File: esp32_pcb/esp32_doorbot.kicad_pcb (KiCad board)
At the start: 2 copper layers, 29.2 x 51.8 mm, 20 parts, among them J1 Conn_01x07_Male, J2 Conn_01x02_Female, J3 Barrel_Jack, J4 WROOM32_1, J5 WROOM32_2, Q1 ZXMP4A16G, U1 L7805

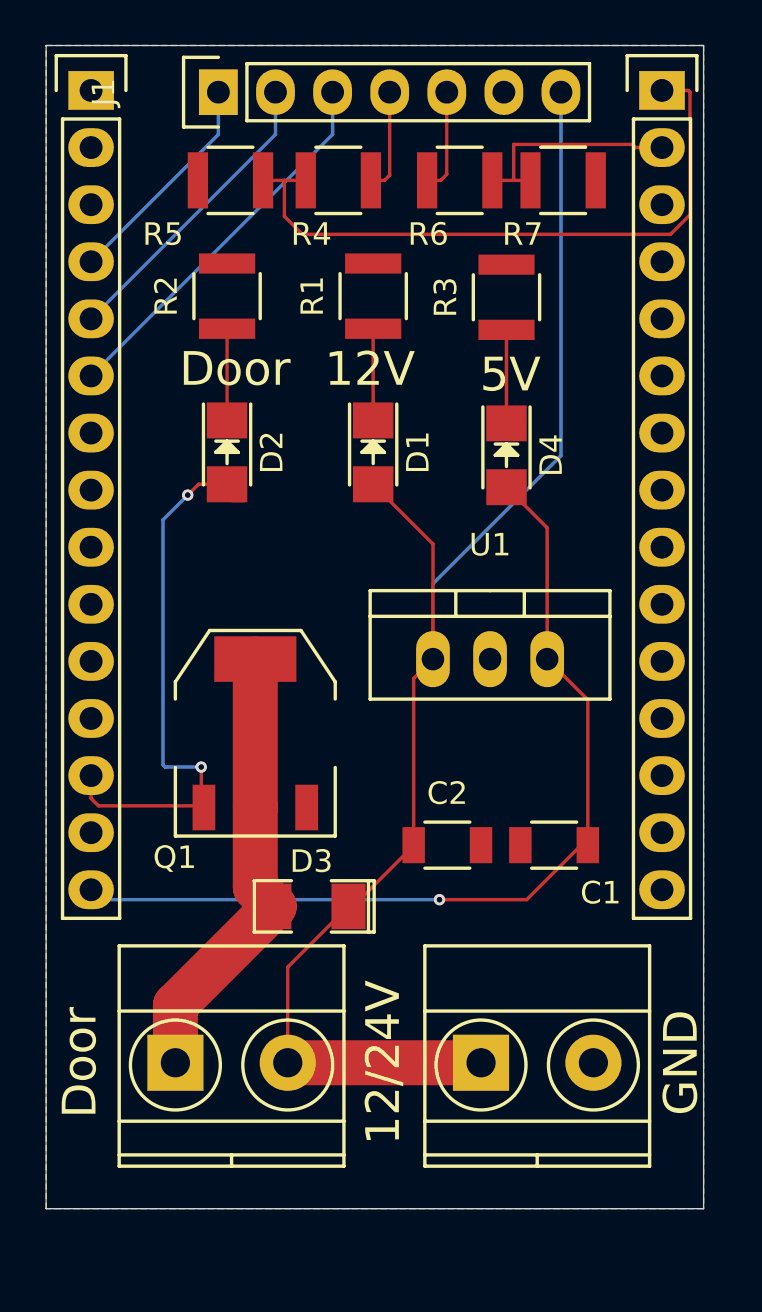
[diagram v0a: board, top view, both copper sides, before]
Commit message: Convert power screw terminal into barrel jack. Convert back pin header to proper JST-ZH connector.
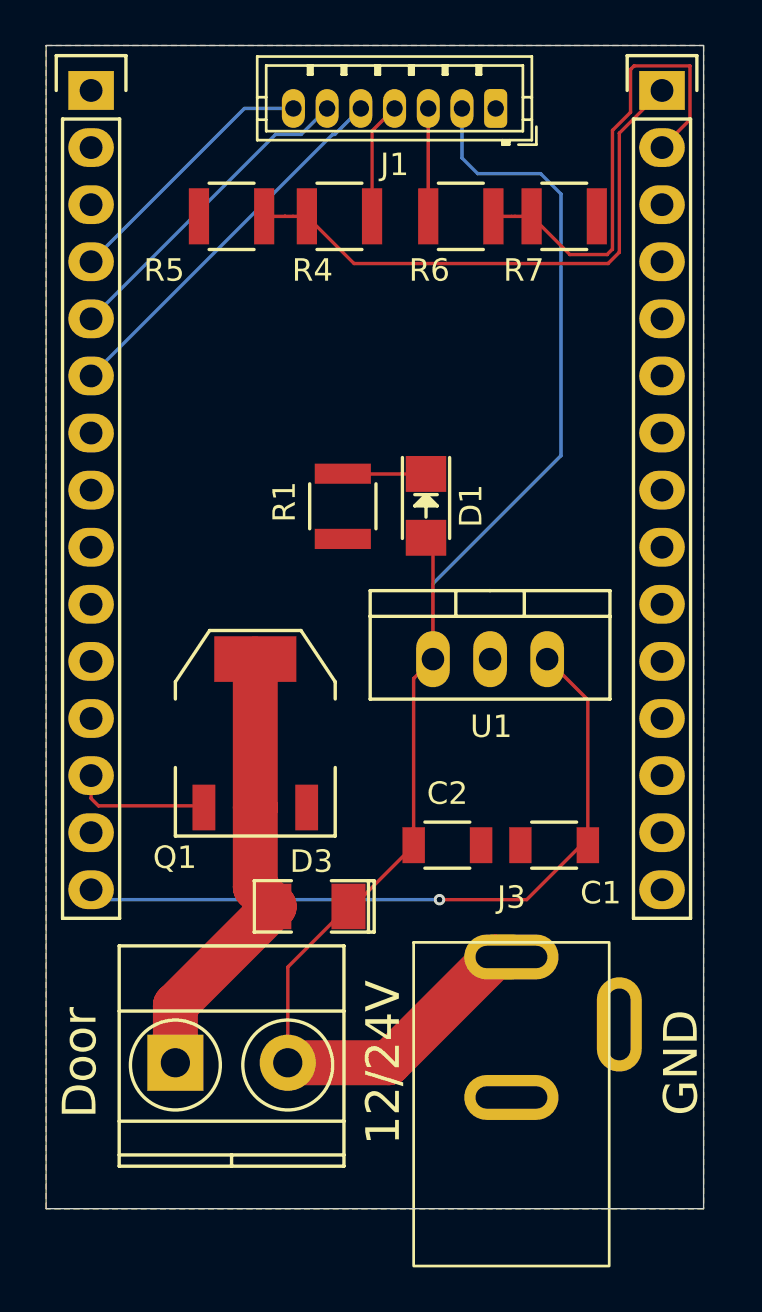
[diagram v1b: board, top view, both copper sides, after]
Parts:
- removed D2, D4: LED, LEDs:LED-1206
- removed R2, R3: 1K, Resistors_SMD:R_1210
- added REF**: Polarity_Center_Positive_6mm_SilkScreen, Symbol:Polarity_Center_Positive_6mm_SilkScreen, B.Cu at (111.2, 128.0)
- J1: footprint Pin_Headers:Pin_Header_Straight_1x07 -> Connector_JST:JST_ZH_B7B-ZR_1x07_P1.50mm_Vertical
- J3: footprint Terminal_Blocks:TerminalBlock_Pheonix_MKDS1.5-2pol -> esp32_doorbot:Tensility 54-00166
- Q1: value ZXMP4A16G -> NDT3055
- R1: value 1K -> 2K
- moved J1 12.4 mm to (118.0, 100.8), turned to 180 degrees
- moved R1 9.45 mm to (111.2, 118.5), turned to -90 degrees
- moved J3 9.14 mm to (118.7, 152.3)
- moved D1 3.34 mm to (114.9, 118.5)
- moved R4 1.60 mm to (111.0, 105.6)
- moved R5 1.60 mm to (106.2, 105.6)
- moved R6 1.60 mm to (116.5, 105.6)
- moved R7 1.60 mm to (121.0, 105.6)
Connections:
- J1 pad 1: 24_32_SWITCH -> GND
- J1 pad 2: READER_LED -> 12V
- J1 pad 3: READER_BUZZ -> WIEGAND_IN1
- J1 pad 5: WIEGAND_IN1 -> READER_BUZZ
- J1 pad 6: GND -> READER_LED
- J1 pad 7: 12V -> 24_32_SWITCH
- J4 pad 1: Net-(J4-Pad1) -> unconnected-(J4-Pin_1-Pad1)
- J4 pad 10: Net-(J4-Pad10) -> unconnected-(J4-Pin_10-Pad10)
- J4 pad 11: Net-(J4-Pad11) -> unconnected-(J4-Pin_11-Pad11)
- J4 pad 12: Net-(J4-Pad12) -> unconnected-(J4-Pin_12-Pad12)
- J4 pad 2: Net-(J4-Pad2) -> unconnected-(J4-Pin_2-Pad2)
- J4 pad 3: Net-(J4-Pad3) -> unconnected-(J4-Pin_3-Pad3)
- J4 pad 7: Net-(J4-Pad7) -> unconnected-(J4-Pin_7-Pad7)
- J4 pad 8: Net-(J4-Pad8) -> unconnected-(J4-Pin_8-Pad8)
- J4 pad 9: Net-(J4-Pad9) -> unconnected-(J4-Pin_9-Pad9)
- J5 pad 10: Net-(J5-Pad10) -> unconnected-(J5-Pin_10-Pad10)
- J5 pad 11: Net-(J5-Pad11) -> unconnected-(J5-Pin_11-Pad11)
- J5 pad 12: Net-(J5-Pad12) -> unconnected-(J5-Pin_12-Pad12)
- J5 pad 13: Net-(J5-Pad13) -> unconnected-(J5-Pin_13-Pad13)
- J5 pad 15: Net-(J5-Pad15) -> unconnected-(J5-Pin_15-Pad15)
- J5 pad 3: Net-(J5-Pad3) -> unconnected-(J5-Pin_3-Pad3)
- J5 pad 4: Net-(J5-Pad4) -> unconnected-(J5-Pin_4-Pad4)
- J5 pad 5: Net-(J5-Pad5) -> unconnected-(J5-Pin_5-Pad5)
- J5 pad 6: Net-(J5-Pad6) -> unconnected-(J5-Pin_6-Pad6)
- J5 pad 7: Net-(J5-Pad7) -> unconnected-(J5-Pin_7-Pad7)
- J5 pad 8: Net-(J5-Pad8) -> unconnected-(J5-Pin_8-Pad8)
- J5 pad 9: Net-(J5-Pad9) -> unconnected-(J5-Pin_9-Pad9)
- Q1 pad 4: LATCH_OUT -> (no net)
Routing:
- net DOOR: track 25.0 -> 6.56 mm, vias 2 -> 0
- net WIEGAND_OUT1: track 9.96 -> 22.2 mm
- net 5V: track 41.0 -> 32.6 mm
- net Net-(D4-Pad1): track 4.16 -> 0.00 mm
- net WIEGAND_OUT2: track 29.0 -> 24.9 mm
- net Net-(D2-Pad1): track 4.08 -> 0.00 mm
- net 12V: track 65.7 -> 68.5 mm
- net 24_32_SWITCH: track 10.4 -> 11.8 mm
- net READER_LED: track 13.5 -> 14.4 mm
- net WIEGAND_IN2: track 4.62 -> 5.21 mm
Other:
- net class Default removed
- board text added: "ESP32 Doorbot v6 By Timm Murray Copyright © 2021 BY-CC"
- board text removed: "12V"
- board text removed: "5V"
- board text removed: "ESP32 Doorbot v5 By Timm Murray Copyright © 2021 BY-CC"
